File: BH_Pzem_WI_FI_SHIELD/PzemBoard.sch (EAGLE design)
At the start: 23 parts, among them J6 8p, J7 8p, U1 DS18B20, U2 esp12

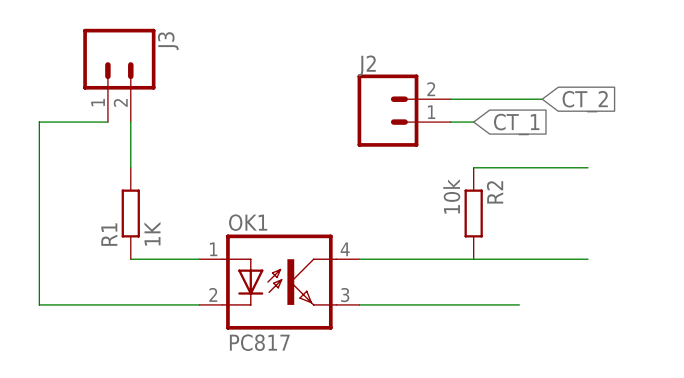
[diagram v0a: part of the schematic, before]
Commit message: pista em falta para o GND
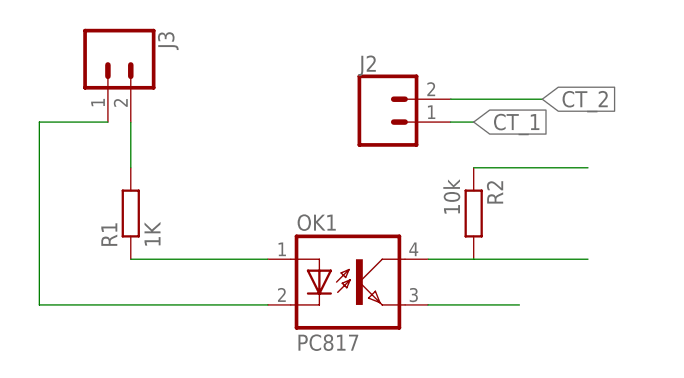
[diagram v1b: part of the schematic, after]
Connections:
- removed net N$2: OK1.EMIT
- net GND: now also OK1.EMIT
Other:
- moved on the sheet: OK1
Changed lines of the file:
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@@
 <grid distance="0.1" unitdist="inch" unit="inch" style="lines" multiple="1" display="no" altdistance="0.01" altunitdist="inch" altunit="inch"/>
 <layers>
-<layer number="1" name="Top" color="4" fill="1" visible="yes" active="no"/>
-<layer number="2" name="Route2" color="1" fill="3" visible="yes" active="no"/>
-<layer number="3" name="Route3" color="4" fill="3" visible="yes" active="no"/>
-<layer number="4" name="Route4" color="1" fill="4" visible="yes" active="no"/>
-<layer number="5" name="Route5" color="4" fill="4" visible="yes" active="no"/>
-<layer number="6" name="Route6" color="1" fill="8" visible="yes" active="no"/>
-<layer number="7" name="Route7" color="4" fill="8" visible="yes" active="no"/>
-<layer number="8" name="Route8" color="1" fill="2" visible="yes" active="no"/>
-<layer number="9" name="Route9" color="4" fill="2" visible="yes" active="no"/>
-<layer number="10" name="Route10" color="1" fill="7" visible="yes" active="no"/>
-<layer number="11" name="Route11" color="4" fill="7" visible="yes" active="no"/>
-<layer number="12" name="Route12" color="1" fill="5" visible="yes" active="no"/>
-<layer number="13" name="Route13" color="4" fill="5" visible="yes" active="no"/>
-<layer number="14" name="Route14" color="1" fill="6" visible="yes" active="no"/>
-<layer number="15" name="Route15" color="4" fill="6" visible="yes" active="no"/>
-<layer number="16" name="Bottom" color="1" fill="1" visible="yes" active="no"/>
-<layer number="17" name="Pads" color="2" fill="1" visible="yes" active="no"/>
-<layer number="18" name="Vias" color="2" fill="1" visible="yes" active="no"/>
-<layer number="19" name="Unrouted" color="6" fill="1" visible="yes" active="no"/>
-<layer number="20" name="Dimension" color="24" fill="1" visible="yes" active="no"/>
-<layer number="21" name="tPlace" color="7" fill="1" visible="yes" active="no"/>
-<layer number="22" name="bPlace" color="7" fill="1" visible="yes" active="no"/>
-<layer number="23" name="tOrigins" color="15" fill="1" visible="yes" active="no"/>
-<layer number="24" name="bOrigins" color="15" fill="1" visible="yes" active="no"/>
-<layer number="25" name="tNames" color="7" fill="1" visible="yes" active="no"/>
-<layer number="26" name="bNames" color="7" fill="1" visible="yes" active="no"/>
-<layer number="27" name="tValues" color="7" fill="1" visible="yes" active="no"/>
-<layer number="28" name="bValues" color="7" fill="1" visible="yes" active="no"/>
+<layer number="1" name="Top" color="4" fill="1" visible="no" active="no"/>
+<layer number="2" name="Route2" color="1" fill="3" visible="no" active="no"/>
+<layer number="3" name="Route3" color="4" fill="3" visible="no" active="no"/>
+<layer number="4" name="Route4" color="1" fill="4" visible="no" active="no"/>
+<layer number="5" name="Route5" color="4" fill="4" visible="no" active="no"/>
+<layer number="6" name="Route6" color="1" fill="8" visible="no" active="no"/>
+<layer number="7" name="Route7" color="4" fill="8" visible="no" active="no"/>
+<layer number="8" name="Route8" color="1" fill="2" visible="no" active="no"/>
+<layer number="9" name="Route9" color="4" fill="2" visible="no" active="no"/>
+<layer number="10" name="Route10" color="1" fill="7" visible="no" active="no"/>
+<layer number="11" name="Route11" color="4" fill="7" visible="no" active="no"/>
+<layer number="12" name="Route12" color="1" fill="5" visible="no" active="no"/>
+<layer number="13" name="Route13" color="4" fill="5" visible="no" active="no"/>
+<layer number="14" name="Route14" color="1" fill="6" visible="no" active="no"/>
+<layer number="15" name="Route15" color="4" fill="6" visible="no" active="no"/>
+<layer number="16" name="Bottom" color="1" fill="1" visible="no" active="no"/>
+<layer number="17" name="Pads" color="2" fill="1" visible="no" active="no"/>
+<layer number="18" name="Vias" color="2" fill="1" visible="no" active="no"/>
+<layer number="19" name="Unrouted" color="6" fill="1" visible="no" active="no"/>
+<layer number="20" name="Dimension" color="24" fill="1" visible="no" active="no"/>
+<layer number="21" name="tPlace" color="7" fill="1" visible="no" active="no"/>
+<layer number="22" name="bPlace" color="7" fill="1" visible="no" active="no"/>
+<layer number="23" name="tOrigins" color="15" fill="1" visible="no" active="no"/>
+<layer number="24" name="bOrigins" color="15" fill="1" visible="no" active="no"/>
+<layer number="25" name="tNames" color="7" fill="1" visible="no" active="no"/>
+<layer number="26" name="bNames" color="7" fill="1" visible="no" active="no"/>
+<layer number="27" name="tValues" color="7" fill="1" visible="no" active="no"/>
+<layer number="28" name="bValues" color="7" fill="1" visible="no" active="no"/>
 <layer number="29" name="tStop" color="7" fill="3" visible="no" active="no"/>
 <layer number="30" name="bStop" color="7" fill="6" visible="no" active="no"/>
@@
 <layer number="35" name="tGlue" color="7" fill="4" visible="no" active="no"/>
 <layer number="36" name="bGlue" color="7" fill="5" visible="no" active="no"/>
-<layer number="37" name="tTest" color="7" fill="1" visible="yes" active="no"/>
-<layer number="38" name="bTest" color="7" fill="1" visible="yes" active="no"/>
+<layer number="37" name="tTest" color="7" fill="1" visible="no" active="no"/>
+<layer number="38" name="bTest" color="7" fill="1" visible="no" active="no"/>
 <layer number="39" name="tKeepout" color="4" fill="11" visible="no" active="no"/>
 <layer number="40" name="bKeepout" color="1" fill="11" visible="no" active="no"/>
@@
 <layer number="44" name="Drills" color="7" fill="1" visible="no" active="no"/>
 <layer number="45" name="Holes" color="7" fill="1" visible="no" active="no"/>
-<layer number="46" name="Milling" color="3" fill="1" visible="yes" active="no"/>
-<layer number="47" name="Measures" color="7" fill="1" visible="yes" active="no"/>
-<layer number="48" name="Document" color="7" fill="1" visible="yes" active="no"/>
-<layer number="49" name="Reference" color="7" fill="1" visible="yes" active="no"/>
-<layer number="50" name="dxf" color="12" fill="1" visible="yes" active="no"/>
-<layer number="51" name="tDocu" color="7" fill="1" visible="yes" active="no"/>
-<layer number="52" name="bDocu" color="7" fill="1" visible="yes" active="no"/>
-<layer number="53" name="tGND_GNDA" color="7" fill="1" visible="yes" active="no"/>
-<layer number="54" name="bGND_GNDA" color="7" fill="1" visible="yes" active="no"/>
-<layer number="56" name="wert" color="7" fill="1" visible="yes" active="no"/>
-<layer number="57" name="tCAD" color="7" fill="1" visible="yes" active="no"/>
-<layer number="59" name="tCarbon" color="7" fill="1" visible="yes" active="no"/>
-<layer number="60" name="bCarbon" color="7" fill="1" visible="yes" active="no"/>
+<layer number="46" name="Milling" color="3" fill="1" visible="no" active="no"/>
+<layer number="47" name="Measures" color="7" fill="1" visible="no" active="no"/>
+<layer number="48" name="Document" color="7" fill="1" visible="no" active="no"/>
+<layer number="49" name="Reference" color="7" fill="1" visible="no" active="no"/>
+<layer number="50" name="dxf" color="12" fill="1" visible="no" active="no"/>
+<layer number="51" name="tDocu" color="7" fill="1" visible="no" active="no"/>
+<layer number="52" name="bDocu" color="7" fill="1" visible="no" active="no"/>
+<layer number="53" name="tGND_GNDA" color="7" fill="1" visible="no" active="no"/>
+<layer number="54" name="bGND_GNDA" color="7" fill="1" visible="no" active="no"/>
+<layer number="56" name="wert" color="7" fill="1" visible="no" active="no"/>
+<layer number="57" name="tCAD" color="7" fill="1" visible="no" active="no"/>
+<layer number="59" name="tCarbon" color="7" fill="1" visible="no" active="no"/>
+<layer number="60" name="bCarbon" color="7" fill="1" visible="no" active="no"/>
 <layer number="88" name="SimResults" color="9" fill="1" visible="yes" active="yes"/>
 <layer number="89" name="SimProbes" color="9" fill="1" visible="yes" active="yes"/>
@@
 <instance part="X3" gate="-4" x="45.72" y="58.42"/>
 <instance part="J1" gate="G$1" x="104.14" y="66.04"/>
-<instance part="OK1" gate="A" x="38.1" y="20.32"/>
+<instance part="OK1" gate="A" x="45.72" y="20.32"/>
 <instance part="U1" gate="G$1" x="213.36" y="88.9"/>
 <instance part="R1" gate="G$1" x="20.32" y="27.94" rot="R90"/>
@@
 <label x="190.5" y="83.82" size="1.778" layer="95" rot="R270" xref="yes"/>
 </segment>
+<segment>
+<pinref part="OK1" gate="A" pin="EMIT"/>
+<wire x1="53.34" y1="17.78" x2="63.5" y2="17.78" width="0.1524" layer="91"/>
+</segment>
 </net>
 <net name="VCC" class="0">
@@
 <pinref part="OK1" gate="A" pin="COL"/>
 <pinref part="R2" gate="G$1" pin="2"/>
-<wire x1="58.42" y1="22.86" x2="45.72" y2="22.86" width="0.1524" layer="91"/>
+<wire x1="58.42" y1="22.86" x2="53.34" y2="22.86" width="0.1524" layer="91"/>
 <wire x1="58.42" y1="22.86" x2="71.12" y2="22.86" width="0.1524" layer="91"/>
 </segment>
@@
 <pinref part="OK1" gate="A" pin="A"/>
 <pinref part="R1" gate="G$1" pin="1"/>
-<wire x1="20.32" y1="22.86" x2="27.94" y2="22.86" width="0.1524" layer="91"/>
+<wire x1="20.32" y1="22.86" x2="35.56" y2="22.86" width="0.1524" layer="91"/>
 </segment>
 </net>
@@
 </segment>
 </net>
-<net name="N$2" class="0">
-<segment>
-<pinref part="OK1" gate="A" pin="EMIT"/>
-<wire x1="45.72" y1="17.78" x2="63.5" y2="17.78" width="0.1524" layer="91"/>
-</segment>
-</net>
 <net name="SIGNAL_GND" class="0">
 <segment>
 <pinref part="OK1" gate="A" pin="C"/>
-<wire x1="27.94" y1="17.78" x2="10.16" y2="17.78" width="0.1524" layer="91"/>
+<wire x1="35.56" y1="17.78" x2="10.16" y2="17.78" width="0.1524" layer="91"/>
 <pinref part="J3" gate="G$1" pin="1"/>
 <wire x1="17.78" y1="38.1" x2="10.16" y2="38.1" width="0.1524" layer="91"/>
